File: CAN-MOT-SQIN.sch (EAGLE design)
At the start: 26 parts, among them U1 TLV760, U2 MCP25625ML, U3 BTM7752G, U4 ATTINY816M, Y1 16MHz

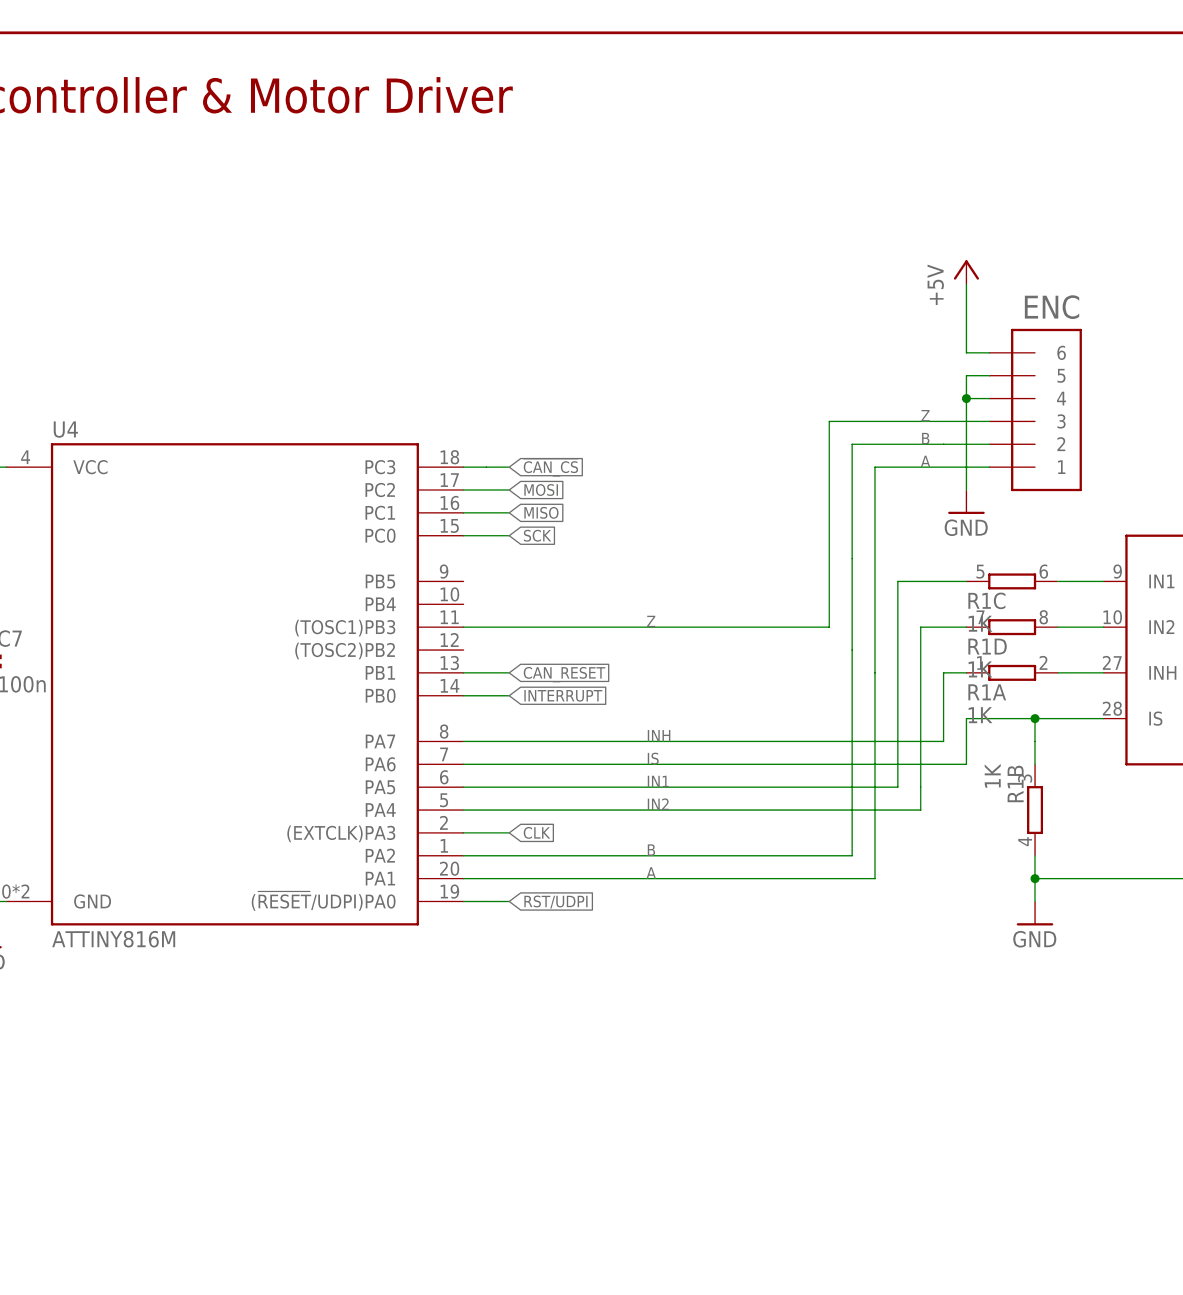
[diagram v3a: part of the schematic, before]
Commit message: Revised with the correct ATTINY816 footprint and external logic for the encoder
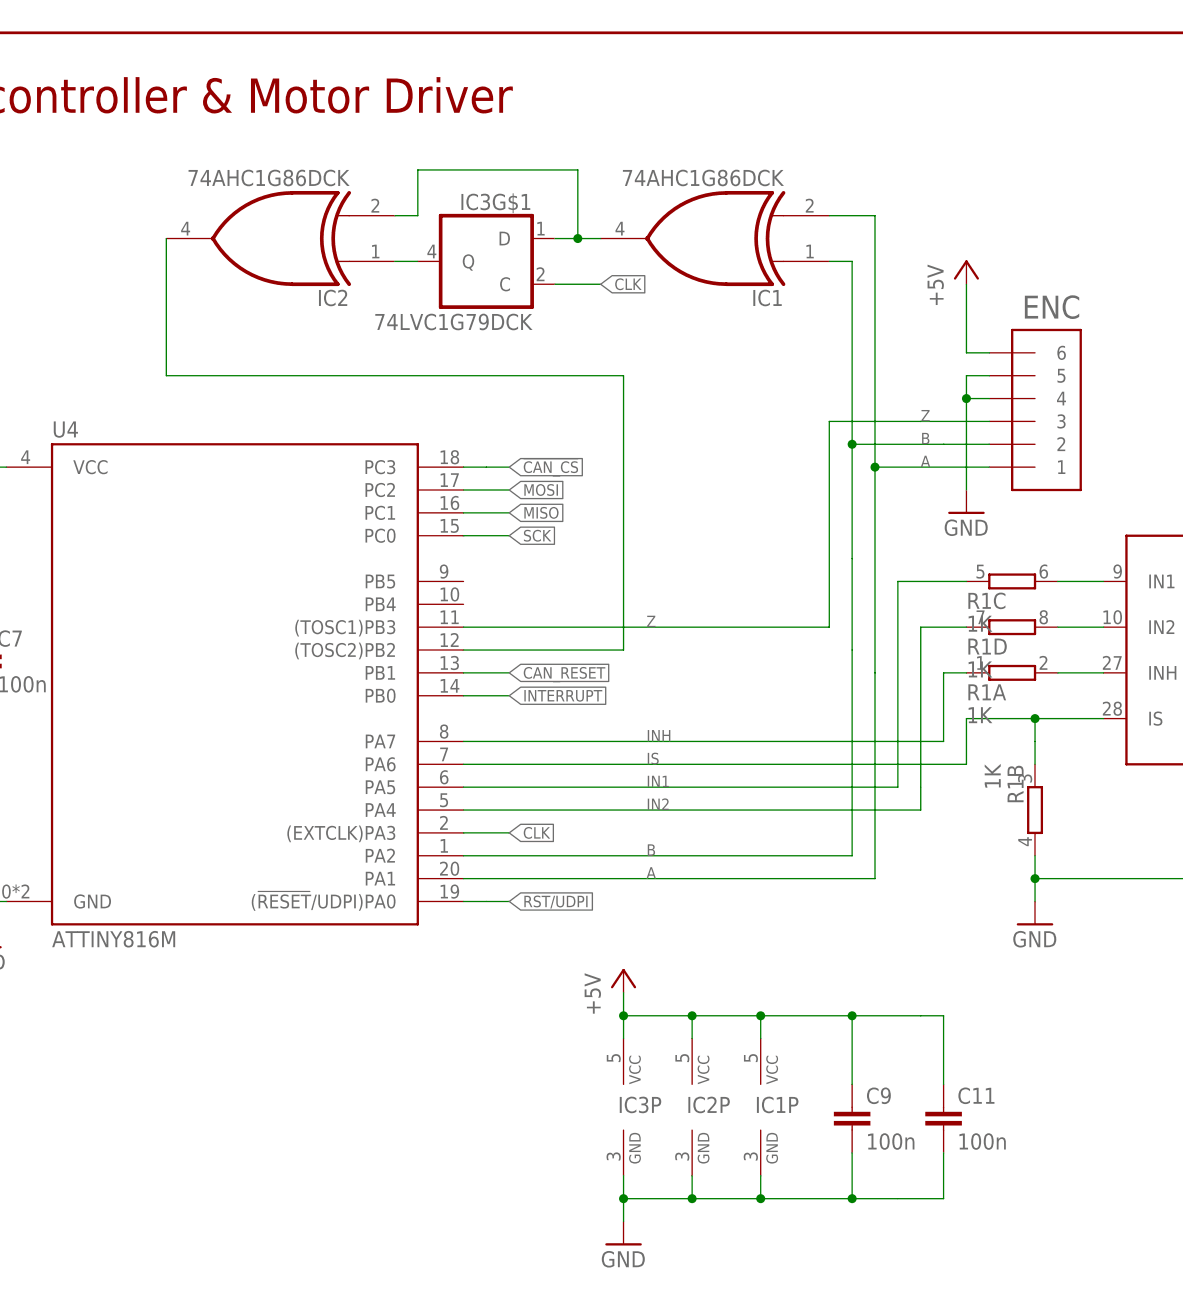
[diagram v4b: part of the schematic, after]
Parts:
- added C11, C9: 100n, resistor:C-EUC0603
- added IC1, IC2: 74AHC1G86DCK, 74xx-little-us:74AHC1G86DCK
- added IC3: 74LVC1G79DCK, 74xx-little-us:74LVC1G79DCK
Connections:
- new net N$4: IC2A.I0, IC3G$1.Q
- new net N$5: IC1A.O, IC2A.I1, IC3G$1.D
- new net N$8: IC2A.O, U4.(TOSC2)PB2
- net +5V: now also C11.1, C9.1, IC1P.VCC, IC2P.VCC, IC3P.VCC
- net A: now also IC1A.I1
- net B: now also IC1A.I0
- net CLK: now also IC3G$1.C
- net GND: now also C11.2, C9.2, IC1P.GND, IC2P.GND, IC3P.GND
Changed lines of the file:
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@@
 <part name="R3" library="resistor" library_urn="urn:adsk.eagle:library:348" deviceset="R-EU_" device="R0603" package3d_urn="urn:adsk.eagle:package:23555/2" value="100K"/>
 <part name="PROG" library="SparkFun-Connectors" library_urn="urn:adsk.eagle:library:513" deviceset="CONN_03" device="LOCK" package3d_urn="urn:adsk.eagle:package:38071/1"/>
+<part name="IC1" library="74xx-little-us" library_urn="urn:adsk.eagle:library:87" deviceset="74*1G86" device="DCK" package3d_urn="urn:adsk.eagle:package:2483/1" technology="AHC" value="74AHC1G86DCK"/>
+<part name="IC2" library="74xx-little-us" library_urn="urn:adsk.eagle:library:87" deviceset="74*1G86" device="DCK" package3d_urn="urn:adsk.eagle:package:2483/1" technology="AHC" value="74AHC1G86DCK"/>
+<part name="IC3" library="74xx-little-us" library_urn="urn:adsk.eagle:library:87" deviceset="74*1G79" device="DCK" package3d_urn="urn:adsk.eagle:package:2483/1" technology="LVC" value="74LVC1G79DCK"/>
+<part name="P+8" library="supply1" library_urn="urn:adsk.eagle:library:371" deviceset="+5V" device=""/>
+<part name="GND7" library="supply1" library_urn="urn:adsk.eagle:library:371" deviceset="GND" device=""/>
+<part name="C9" library="resistor" library_urn="urn:adsk.eagle:library:348" deviceset="C-EU" device="C0603" package3d_urn="urn:adsk.eagle:package:23616/2" value="100n"/>
+<part name="C11" library="resistor" library_urn="urn:adsk.eagle:library:348" deviceset="C-EU" device="C0603" package3d_urn="urn:adsk.eagle:package:23616/2" value="100n"/>
 </parts>
 <sheets>
@@
 <instance part="R3" gate="G$1" x="177.8" y="60.96" rot="R90"/>
 <instance part="PROG" gate="J$1" x="243.84" y="167.64" rot="MR0"/>
+<instance part="IC1" gate="A" x="101.6" y="119.38" rot="R180"/>
+<instance part="IC2" gate="A" x="53.34" y="119.38" rot="R180"/>
+<instance part="IC3" gate="P" x="91.44" y="22.86"/>
+<instance part="IC3" gate="G$1" x="76.2" y="116.84" rot="MR0"/>
+<instance part="P+8" gate="1" x="91.44" y="38.1"/>
+<instance part="GND7" gate="1" x="91.44" y="7.62"/>
+<instance part="IC2" gate="P" x="99.06" y="22.86"/>
+<instance part="IC1" gate="P" x="106.68" y="22.86"/>
+<instance part="C9" gate="G$1" x="116.84" y="22.86"/>
+<instance part="C11" gate="G$1" x="127" y="22.86"/>
 </instances>
 <busses>
@@
 <pinref part="U4" gate="G$1" pin="(EXTCLK)PA3"/>
 <wire x1="73.66" y1="53.34" x2="78.74" y2="53.34" width="0.1524" layer="91"/>
+</segment>
+<segment>
+<pinref part="IC3" gate="G$1" pin="C"/>
+<wire x1="83.82" y1="114.3" x2="88.9" y2="114.3" width="0.1524" layer="91"/>
+<label x="88.9" y="114.3" size="1.27" layer="95" xref="yes"/>
 </segment>
 </net>
@@
 <pinref part="GND6" gate="1" pin="GND"/>
 </segment>
+<segment>
+<pinref part="IC3" gate="P" pin="GND"/>
+<pinref part="GND7" gate="1" pin="GND"/>
+<wire x1="91.44" y1="10.16" x2="91.44" y2="12.7" width="0.1524" layer="91"/>
+<pinref part="IC2" gate="P" pin="GND"/>
+<wire x1="91.44" y1="12.7" x2="91.44" y2="15.24" width="0.1524" layer="91"/>
+<wire x1="91.44" y1="12.7" x2="99.06" y2="12.7" width="0.1524" layer="91"/>
+<wire x1="99.06" y1="12.7" x2="99.06" y2="15.24" width="0.1524" layer="91"/>
+<junction x="91.44" y="12.7"/>
+<pinref part="IC1" gate="P" pin="GND"/>
+<wire x1="99.06" y1="12.7" x2="106.68" y2="12.7" width="0.1524" layer="91"/>
+<wire x1="106.68" y1="12.7" x2="106.68" y2="15.24" width="0.1524" layer="91"/>
+<junction x="99.06" y="12.7"/>
+<pinref part="C9" gate="G$1" pin="2"/>
+<wire x1="106.68" y1="12.7" x2="116.84" y2="12.7" width="0.1524" layer="91"/>
+<wire x1="116.84" y1="12.7" x2="116.84" y2="17.78" width="0.1524" layer="91"/>
+<junction x="106.68" y="12.7"/>
+<wire x1="116.84" y1="12.7" x2="121.92" y2="12.7" width="0.1524" layer="91"/>
+<junction x="116.84" y="12.7"/>
+<pinref part="C11" gate="G$1" pin="2"/>
+<wire x1="121.92" y1="12.7" x2="127" y2="12.7" width="0.1524" layer="91"/>
+<wire x1="127" y1="12.7" x2="127" y2="17.78" width="0.1524" layer="91"/>
+</segment>
 </net>
 <net name="CANH" class="0">
@@
 <wire x1="129.54" y1="106.68" x2="129.54" y2="114.3" width="0.1524" layer="91"/>
 <pinref part="P+5" gate="1" pin="+5V"/>
+</segment>
+<segment>
+<pinref part="IC3" gate="P" pin="VCC"/>
+<pinref part="P+8" gate="1" pin="+5V"/>
+<wire x1="91.44" y1="35.56" x2="91.44" y2="33.02" width="0.1524" layer="91"/>
+<wire x1="91.44" y1="33.02" x2="91.44" y2="30.48" width="0.1524" layer="91"/>
+<wire x1="91.44" y1="33.02" x2="99.06" y2="33.02" width="0.1524" layer="91"/>
+<junction x="91.44" y="33.02"/>
+<pinref part="IC2" gate="P" pin="VCC"/>
+<wire x1="99.06" y1="33.02" x2="99.06" y2="30.48" width="0.1524" layer="91"/>
+<pinref part="IC1" gate="P" pin="VCC"/>
+<wire x1="99.06" y1="33.02" x2="106.68" y2="33.02" width="0.1524" layer="91"/>
+<wire x1="106.68" y1="33.02" x2="106.68" y2="30.48" width="0.1524" layer="91"/>
+<junction x="99.06" y="33.02"/>
+<pinref part="C9" gate="G$1" pin="1"/>
+<wire x1="106.68" y1="33.02" x2="116.84" y2="33.02" width="0.1524" layer="91"/>
+<wire x1="116.84" y1="33.02" x2="116.84" y2="25.4" width="0.1524" layer="91"/>
+<junction x="106.68" y="33.02"/>
+<wire x1="116.84" y1="33.02" x2="124.46" y2="33.02" width="0.1524" layer="91"/>
+<junction x="116.84" y="33.02"/>
+<pinref part="C11" gate="G$1" pin="1"/>
+<wire x1="124.46" y1="33.02" x2="127" y2="33.02" width="0.1524" layer="91"/>
+<wire x1="127" y1="33.02" x2="127" y2="25.4" width="0.1524" layer="91"/>
 </segment>
 </net>
@@
 <wire x1="73.66" y1="48.26" x2="119.38" y2="48.26" width="0.1524" layer="91"/>
 <wire x1="119.38" y1="48.26" x2="119.38" y2="71.12" width="0.1524" layer="91"/>
+<pinref part="IC1" gate="A" pin="I1"/>
+<wire x1="114.3" y1="121.92" x2="119.38" y2="121.92" width="0.1524" layer="91"/>
+<wire x1="119.38" y1="121.92" x2="119.38" y2="93.98" width="0.1524" layer="91"/>
+<junction x="119.38" y="93.98"/>
 </segment>
 </net>
@@
 <wire x1="73.66" y1="50.8" x2="116.84" y2="50.8" width="0.1524" layer="91"/>
 <wire x1="116.84" y1="50.8" x2="116.84" y2="73.66" width="0.1524" layer="91"/>
+<wire x1="116.84" y1="96.52" x2="116.84" y2="116.84" width="0.1524" layer="91"/>
+<junction x="116.84" y="96.52"/>
+<pinref part="IC1" gate="A" pin="I0"/>
+<wire x1="116.84" y1="116.84" x2="114.3" y2="116.84" width="0.1524" layer="91"/>
 </segment>
 </net>
@@
 </segment>
 </net>
+<net name="N$4" class="0">
+<segment>
+<pinref part="IC2" gate="A" pin="I0"/>
+<pinref part="IC3" gate="G$1" pin="Q"/>
+<wire x1="68.58" y1="116.84" x2="66.04" y2="116.84" width="0.1524" layer="91"/>
+</segment>
+</net>
+<net name="N$5" class="0">
+<segment>
+<pinref part="IC1" gate="A" pin="O"/>
+<pinref part="IC3" gate="G$1" pin="D"/>
+<wire x1="83.82" y1="119.38" x2="86.36" y2="119.38" width="0.1524" layer="91"/>
+<pinref part="IC2" gate="A" pin="I1"/>
+<wire x1="86.36" y1="119.38" x2="88.9" y2="119.38" width="0.1524" layer="91"/>
+<wire x1="66.04" y1="121.92" x2="68.58" y2="121.92" width="0.1524" layer="91"/>
+<wire x1="68.58" y1="121.92" x2="68.58" y2="127" width="0.1524" layer="91"/>
+<wire x1="68.58" y1="127" x2="86.36" y2="127" width="0.1524" layer="91"/>
+<wire x1="86.36" y1="127" x2="86.36" y2="119.38" width="0.1524" layer="91"/>
+<junction x="86.36" y="119.38"/>
+</segment>
+</net>
+<net name="N$8" class="0">
+<segment>
+<pinref part="IC2" gate="A" pin="O"/>
+<wire x1="40.64" y1="119.38" x2="40.64" y2="104.14" width="0.1524" layer="91"/>
+<wire x1="40.64" y1="104.14" x2="91.44" y2="104.14" width="0.1524" layer="91"/>
+<pinref part="U4" gate="G$1" pin="(TOSC2)PB2"/>
+<wire x1="91.44" y1="104.14" x2="91.44" y2="73.66" width="0.1524" layer="91"/>
+<wire x1="91.44" y1="73.66" x2="73.66" y2="73.66" width="0.1524" layer="91"/>
+</segment>
+</net>
